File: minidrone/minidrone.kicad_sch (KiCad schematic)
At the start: 52 parts, among them J1 Conn_01x10, J2 OUT, J3 EXT GATE, J4 GATE, Q6 BC377, Q7 BC377, Q8 BC377, Q9 BC377, SW6 GATE_LATCH, U1 TL072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

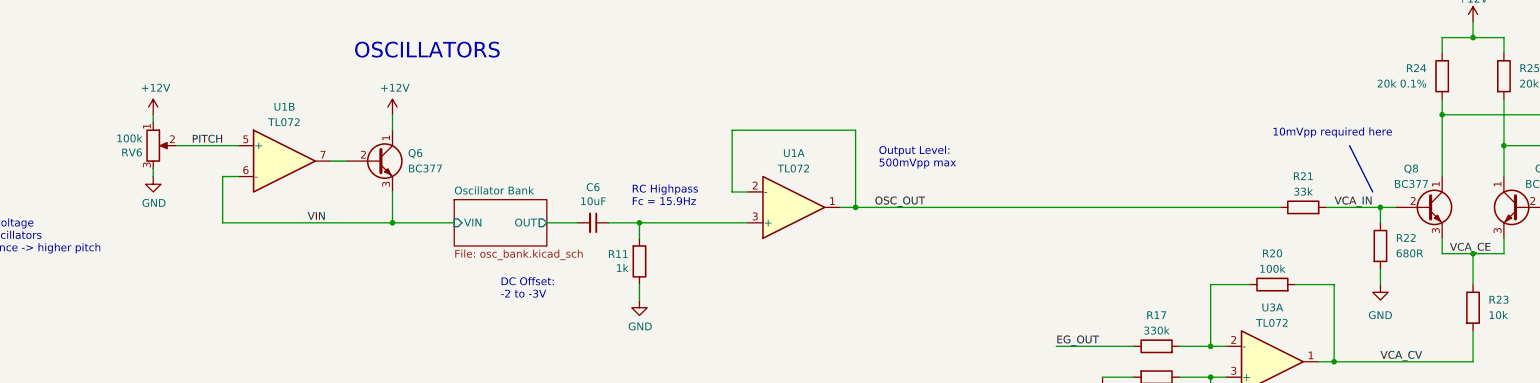
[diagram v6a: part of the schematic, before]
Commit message: Fix schematic issues identified in first production run. PCB fixes TODO!
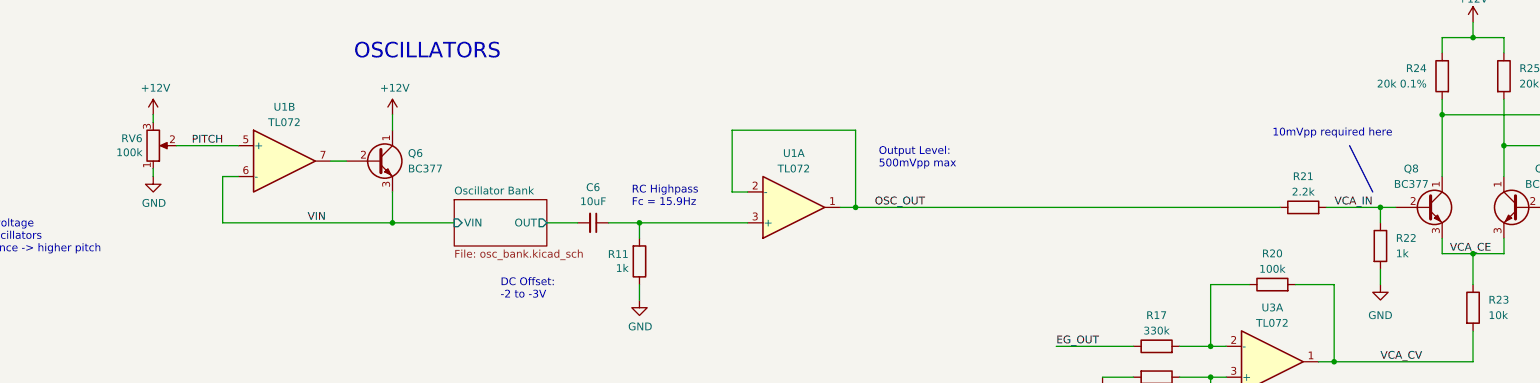
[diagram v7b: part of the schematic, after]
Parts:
- R21: value 33k -> 2.2k
- R22: value 680R -> 1k
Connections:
- net +12V: now also RV6.3; no longer RV6.1
- net GND: now also RV6.1; no longer RV6.3
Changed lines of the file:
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@@
     (pin "1")
   )
-  (symbol (lib_id "Device:R_POT") (at 67.31 80.01 0) (unit 1)
-    (in_bom yes) (on_board yes)
-    (property "Reference" "RV6" (id 0) (at 65.5574 81.1784 0)
+  (symbol (lib_id "Device:R_POT") (at 67.31 80.01 0) (mirror x) (unit 1)
+    (in_bom yes) (on_board yes)
+    (property "Reference" "RV6" (id 0) (at 65.5574 78.8416 0)
       (effects (font (size 1.27 1.27)) (justify right))
     )
-    (property "Value" "100k" (id 1) (at 65.5574 78.867 0)
+    (property "Value" "100k" (id 1) (at 65.5574 81.153 0)
       (effects (font (size 1.27 1.27)) (justify right))
     )
@@
     (in_bom yes) (on_board yes)
     (property "Reference" "R21" (id 0) (at 256.54 85.09 90))
-    (property "Value" "33k" (id 1) (at 256.54 87.63 90))
+    (property "Value" "2.2k" (id 1) (at 256.54 87.63 90))
     (property "Footprint" "Resistor_THT:R_Axial_DIN0207_L6.3mm_D2.5mm_P10.16mm_Horizontal" (id 2) (at 256.54 91.948 90)
       (effects (font (size 1.27 1.27)) hide)
@@
       (effects (font (size 1.27 1.27)) (justify left))
     )
-    (property "Value" "680R" (id 1) (at 271.78 97.7899 0)
+    (property "Value" "1k" (id 1) (at 271.78 97.7899 0)
       (effects (font (size 1.27 1.27)) (justify left))
     )
@@
     )
     (path "/e1f16118-a2c4-4549-a045-798105ac5650"
-      (reference "R21") (unit 1) (value "33k") (footprint "Resistor_THT:R_Axial_DIN0207_L6.3mm_D2.5mm_P10.16mm_Horizontal")
+      (reference "R21") (unit 1) (value "2.2k") (footprint "Resistor_THT:R_Axial_DIN0207_L6.3mm_D2.5mm_P10.16mm_Horizontal")
     )
     (path "/fb29bb2e-2194-4ad7-acf8-dc89f43e2bdb"
-      (reference "R22") (unit 1) (value "680R") (footprint "Resistor_THT:R_Axial_DIN0207_L6.3mm_D2.5mm_P10.16mm_Horizontal")
+      (reference "R22") (unit 1) (value "1k") (footprint "Resistor_THT:R_Axial_DIN0207_L6.3mm_D2.5mm_P10.16mm_Horizontal")
     )
     (path "/a1e57bd1-ff8d-4f6f-b5bc-d8e21ebe9c29"
